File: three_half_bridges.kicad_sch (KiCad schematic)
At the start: 38 parts, among them J1 Conn_01x06_Pin, J2 Conn_01x06_Pin, J3 Conn_01x06_Pin, J4 Current Sense, J5 Conn_01x01_Socket, J6 Conn_01x01_Socket, J7 Conn_01x01_Socket, J8 Conn_01x01_Socket, J9 Conn_01x01_Socket, Q1 Q_NMOS_GDS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

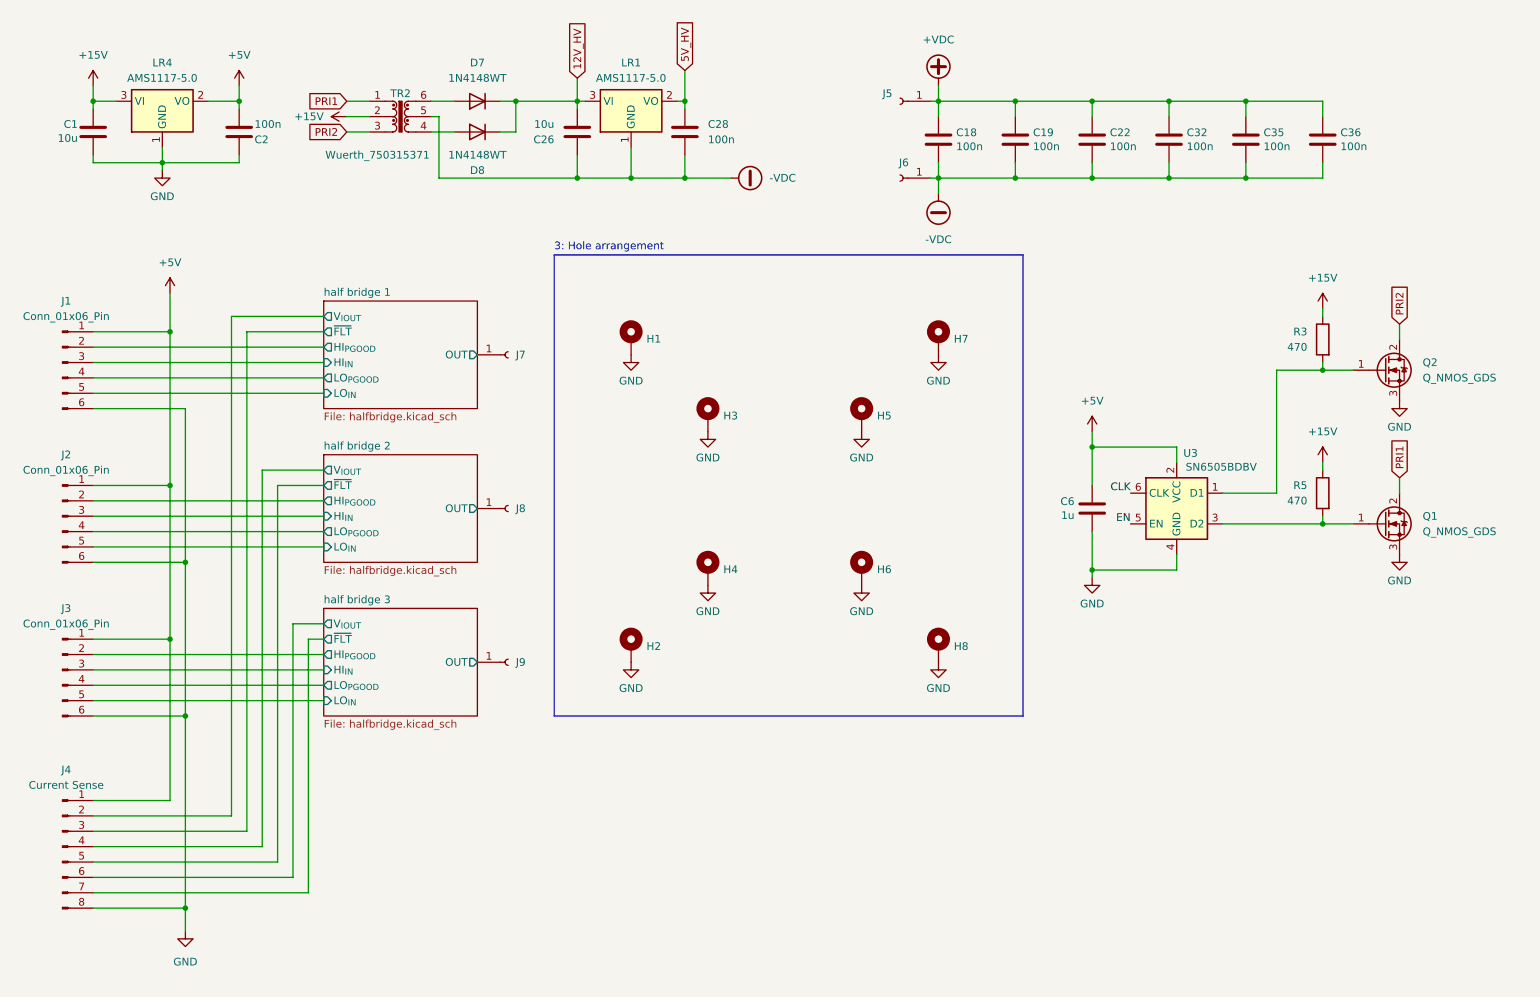
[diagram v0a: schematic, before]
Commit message: Updated LDO footrprint to use the SOT89 LM78L05 (issue 10); moved high side local regulators closer to digital isolator ICs (issue 10); pushed digital isolator ICs further to the allow room for LRs (issue 10); changed designator letter for zener diodes to Z to make it easier when hand soldering (issue 5) Updated footprints from placeholders (most of the diodes) to actual real component choices updated resistor values for BOM consolidation (220, 1k) moved resistor related to PGOOD for more optimal routing w/ minimal impact to function Changed structure of isolated driver design to use voltage doubler and 6505 or similar IC directly (issue 7,8,13) Only 5VDC is required for low voltage side, although several amps may be required depending on gate drive requirements Updated transformer footprint for more common 7.5mm by 2.5mm spacing, several 1:1.1 to 1:1.5 transformers are avilable with such spacing (issue 7) Moved Q8 designator back to correct place along with others that were mislocated somehow... Fixed placement of some footprints that were slightly off or not aligned to 0.25mm grid Replaced specific SO8 MOSFET driver with choose-your-own generic. I am personally using some cheapo LCSC TI 27523 clones (issue 11) added EVEN MORE VIAS!!!! thermal vias on not current sensitive pins to make soldering easier Added artwork (issue 6)
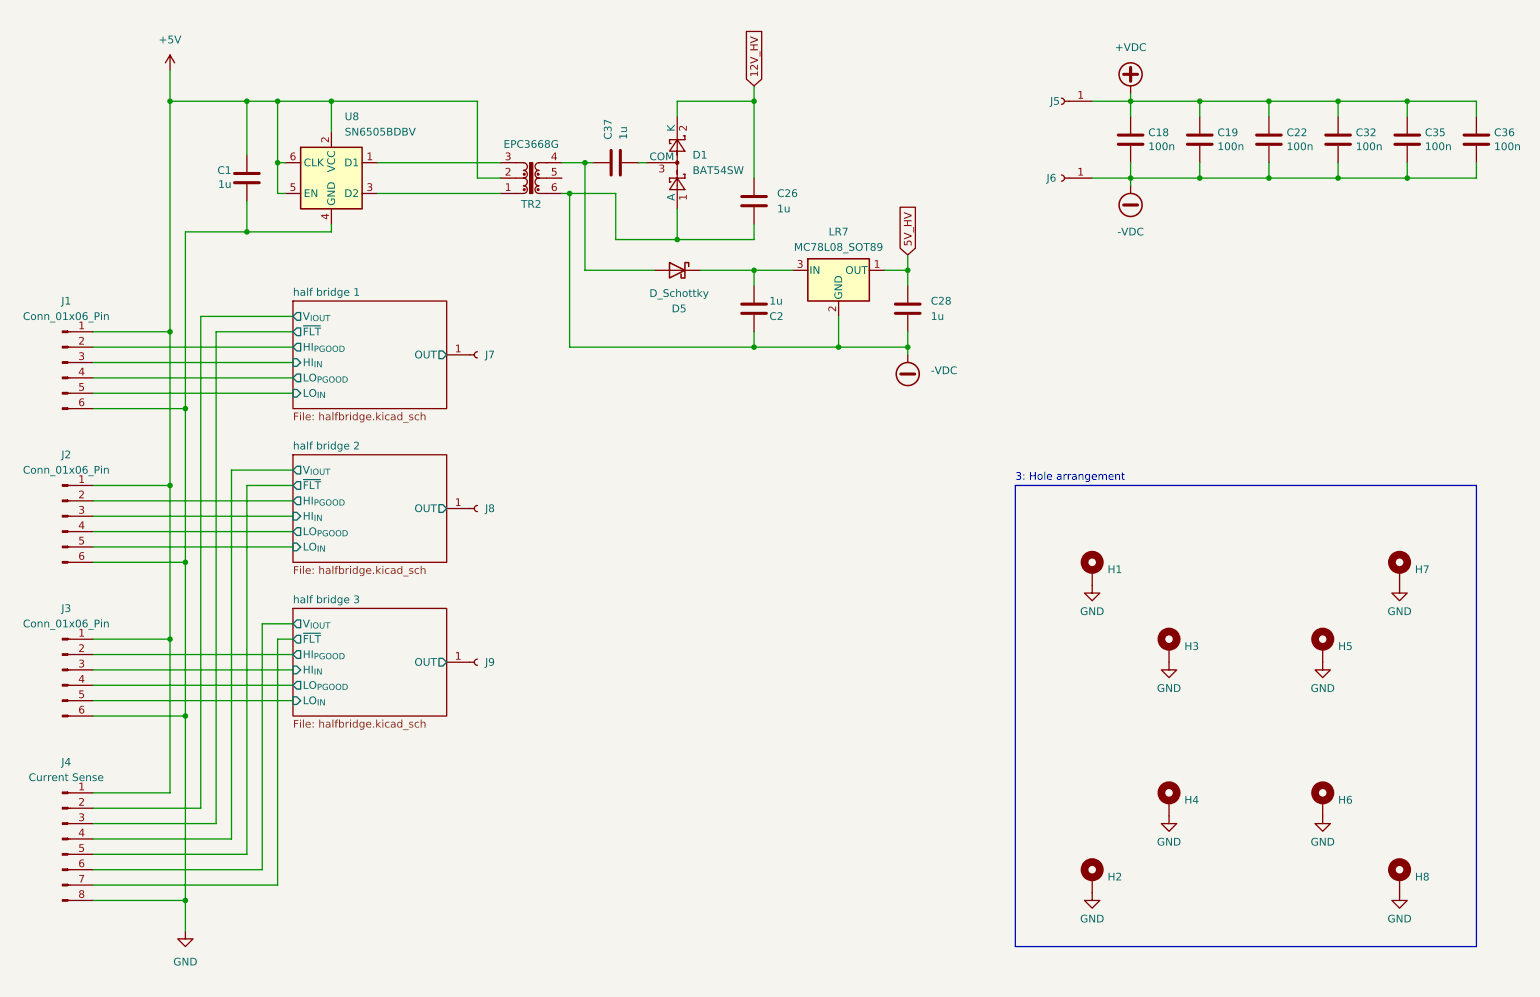
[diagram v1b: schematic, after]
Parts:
- removed C6: 1u, Capacitor_SMD:C_0805_2012Metric, symbol Device:C
- removed D7, D8: 1N4148WT, Diode_SMD:D_SOD-128, symbol Diode:1N4148WT
- removed LR1, LR4: AMS1117-5.0, Package_TO_SOT_SMD:SOT-89-3, symbol Regulator_Linear:AMS1117-5.0
- removed Q1, Q2: Q_NMOS_GDS, Package_TO_SOT_SMD:SOT-89-3, symbol Device:Q_NMOS_GDS
- removed R3, R5: 470, Resistor_SMD:R_0603_1608Metric, symbol Device:R
- removed U3: SN6505BDBV, Package_TO_SOT_SMD:SOT-23-6, symbol Power_Management:SN6505BDBV
- added C37: 1u, Capacitor_SMD:C_0603_1608Metric, symbol Device:C
- added D1: BAT54SW, Package_TO_SOT_SMD:SOT-323_SC-70, symbol Diode:BAT54SW
- added D5: D_Schottky, Diode_SMD:D_SOD-123, symbol Device:D_Schottky
- added LR7: MC78L08_SOT89, Package_TO_SOT_SMD:SOT-89-3, symbol Regulator_Linear:MC78L08_SOT89
- added U8: SN6505BDBV, Package_TO_SOT_SMD:SOT-23-6, symbol Power_Management:SN6505BDBV
- C1, C26: value 10u -> 1u; footprint Capacitor_SMD:C_0805_2012Metric -> Capacitor_SMD:C_0603_1608Metric
- C2, C28: value 100n -> 1u
- TR2: value Wuerth_750315371 -> EPC3668G; footprint Transformer_SMD:Transformer_Wuerth_750315371 -> Transformer_SMD:Pulse_PA2004NL
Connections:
- net +15V is gone; now on net +5V: C1.2, TR2.2
- net +5V: now also U8.2 (VCC), U8.5 (EN), U8.6 (CLK); no longer C2.2
- net -VDC: now also C2.1, C26.2, TR2.6, D1.1 (A), LR7.2 (GND); no longer C26.1, TR2.5
- net 12V_HV: now also C26.1, D1.2 (K); no longer C26.2
- net 5V_HV: now also LR7.1 (OUT)
- net GND: now also U8.4 (GND); no longer C2.1
- net at TR2.4: now also C37.1, D5.2 (A)
- net PRI1: no longer names the net of TR2.1
- net PRI1: now also U8.3 (D2)
- net PRI2: no longer names the net of TR2.3
- net PRI2: now also U8.1 (D1)
- new net: C2.2, D5.1 (K), LR7.3 (IN)
- new net: C37.2, D1.3 (COM)
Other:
- moved on the sheet: C1, C18, C19, C2, C22, C26, C28, C32, C35, C36, H1, H2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

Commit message: forgot to save and close prior to last commit
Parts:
- added J10: Conn_01x02_Pin, Connector_JST:JST_XH_B2B-XH-AM_1x02_P2.50mm_Vertical, symbol Connector:Conn_01x02_Pin
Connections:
- net +5V: now also J10.1 (Pin_1)
- net GND: now also J10.2 (Pin_2)
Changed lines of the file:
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@@
+	)
+	(junction
+		(at 40.64 46.99)
+		(diameter 0)
+		(color 0 0 0 0)
 	)
 	(junction
@@
 	(wire
 		(pts
+			(xy 25.4 25.4) (xy 38.1 25.4)
+		)
+		(stroke
+			(width 0)
+			(type default)
+		)
+	)
+	(wire
+		(pts
 			(xy 50.8 25.4) (xy 55.88 25.4)
 		)
@@
 	(wire
 		(pts
+			(xy 40.64 27.94) (xy 40.64 46.99)
+		)
+		(stroke
+			(width 0)
+			(type default)
+		)
+	)
+	(wire
+		(pts
 			(xy 25.4 99.06) (xy 58.42 99.06)
 		)
@@
 		(pts
 			(xy 40.64 76.2) (xy 40.64 101.6)
+		)
+		(stroke
+			(width 0)
+			(type default)
+		)
+	)
+	(wire
+		(pts
+			(xy 25.4 27.94) (xy 40.64 27.94)
 		)
 		(stroke
@@
 					(unit 1)
 				)
+			)
+		)
+	)
+	(symbol
+		(lib_id "Connector:Conn_01x02_Pin")
+		(at 20.32 25.4 0)
+		(unit 1)
+		(exclude_from_sim no)
+		(in_bom yes)
+		(on_board yes)
+		(dnp no)
+		(fields_autoplaced yes)
+		(property "Reference" "J10"
+			(at 20.955 20.32 0)
+			(effects
+				(font
+					(size 1.27 1.27)
+				)
+			)
+		)
+		(property "Value" "Conn_01x02_Pin"
+			(at 20.955 22.86 0)
+			(effects
+				(font
+					(size 1.27 1.27)
+				)
+			)
+		)
+		(property "Footprint" "Connector_JST:JST_XH_B2B-XH-AM_1x02_P2.50mm_Vertical"
+			(at 20.32 25.4 0)
+			(effects
+				(font
+					(size 1.27 1.27)
+				)
+				(hide yes)
+			)
+		)
+		(property "Datasheet" "~"
+			(at 20.32 25.4 0)
+			(effects
+				(font
+					(size 1.27 1.27)
+				)
+				(hide yes)
+			)
+		)
+		(property "Description" "Generic connector, single row, 01x02, script generated"
+			(at 20.32 25.4 0)
+			(effects
+				(font
+					(size 1.27 1.27)
+				)
+				(hide yes)
+			)
+		)
+		(pin "2"
+		)
+		(pin "1"
+		)
+		(instances
+			(project ""
+				(path "/93b08510-115c-4f21-9eb2-db10547c6f8e"
+					(reference "J10")
+					(unit 1)
+				)

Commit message: updated footprint for terminal blocks to use AMT0450028DB0000G‎
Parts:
- J5, J6, J7, J8, J9: footprint TerminalBlock_MetzConnect:TerminalBlock_MetzConnect_360425_1x01_Horizontal_ScrewM4.0_Boxed -> Library:AMT0450028DB0000G
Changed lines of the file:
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@@
 			)
 		)
-		(property "Footprint" "TerminalBlock_MetzConnect:TerminalBlock_MetzConnect_360425_1x01_Horizontal_ScrewM4.0_Boxed"
+		(property "Footprint" "Library:AMT0450028DB0000G"
 			(at 88.9 118.11 0)
 			(effects
@@
 			)
 		)
-		(property "Footprint" "TerminalBlock_MetzConnect:TerminalBlock_MetzConnect_360425_1x01_Horizontal_ScrewM4.0_Boxed"
+		(property "Footprint" "Library:AMT0450028DB0000G"
 			(at 88.9 92.71 0)
 			(effects
@@
 			)
 		)
-		(property "Footprint" "TerminalBlock_MetzConnect:TerminalBlock_MetzConnect_360425_1x01_Horizontal_ScrewM4.0_Boxed"
+		(property "Footprint" "Library:AMT0450028DB0000G"
 			(at 185.42 25.4 0)
 			(effects
@@
 			)
 		)
-		(property "Footprint" "TerminalBlock_MetzConnect:TerminalBlock_MetzConnect_360425_1x01_Horizontal_ScrewM4.0_Boxed"
+		(property "Footprint" "Library:AMT0450028DB0000G"
 			(at 185.42 38.1 0)
 			(effects
@@
 			)
 		)
-		(property "Footprint" "TerminalBlock_MetzConnect:TerminalBlock_MetzConnect_360425_1x01_Horizontal_ScrewM4.0_Boxed"
+		(property "Footprint" "Library:AMT0450028DB0000G"
 			(at 88.9 67.31 0)
 			(effects

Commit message: beginings of the implementation of the 10 open issues
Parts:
- LR7: value MC78L08_SOT89 -> MC78L05_SOT89
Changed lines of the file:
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@@
 			)
 		)
-		(property "Value" "MC78L08_SOT89"
+		(property "Value" "MC78L05_SOT89"
 			(at 148.59 49.53 0)
 			(effects
@@
 			)
 		)
-		(property "Description" "Positive 100mA 30V Linear Regulator, Fixed Output 8V, SOT-89"
+		(property "Description" "Positive 100mA 30V Linear Regulator, Fixed Output 5V, SOT-89"
 			(at 148.59 53.34 0)
 			(effects

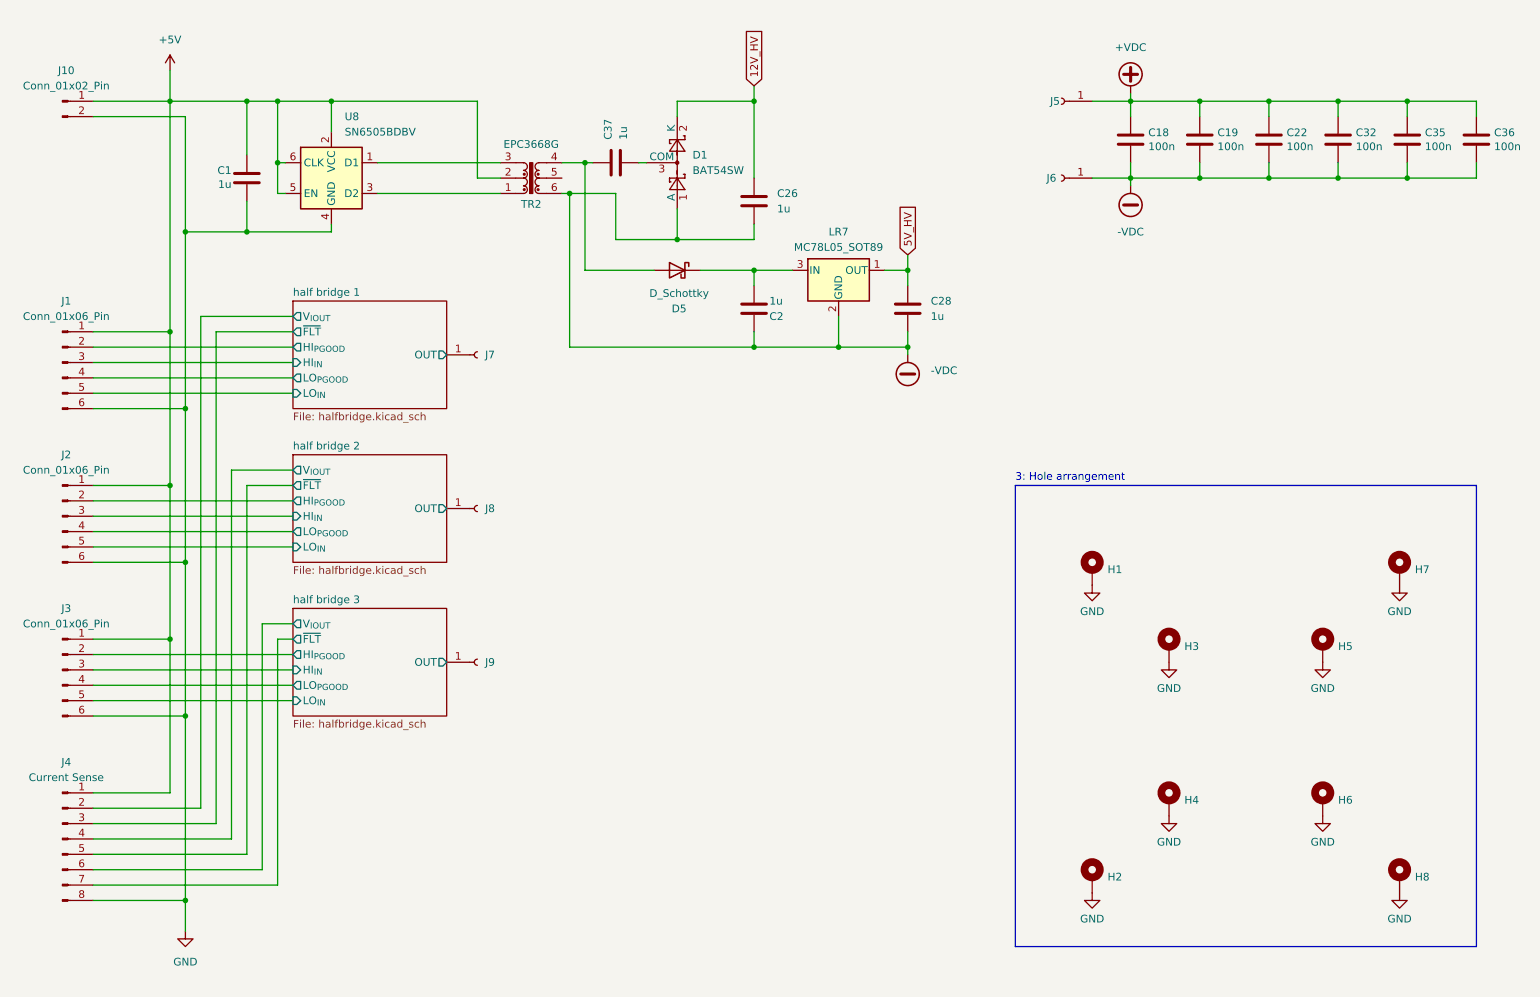
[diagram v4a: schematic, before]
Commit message: fixed many issues from previous itteration, added design rule checks to enforce minumum 2mm clearence between LV and HV side
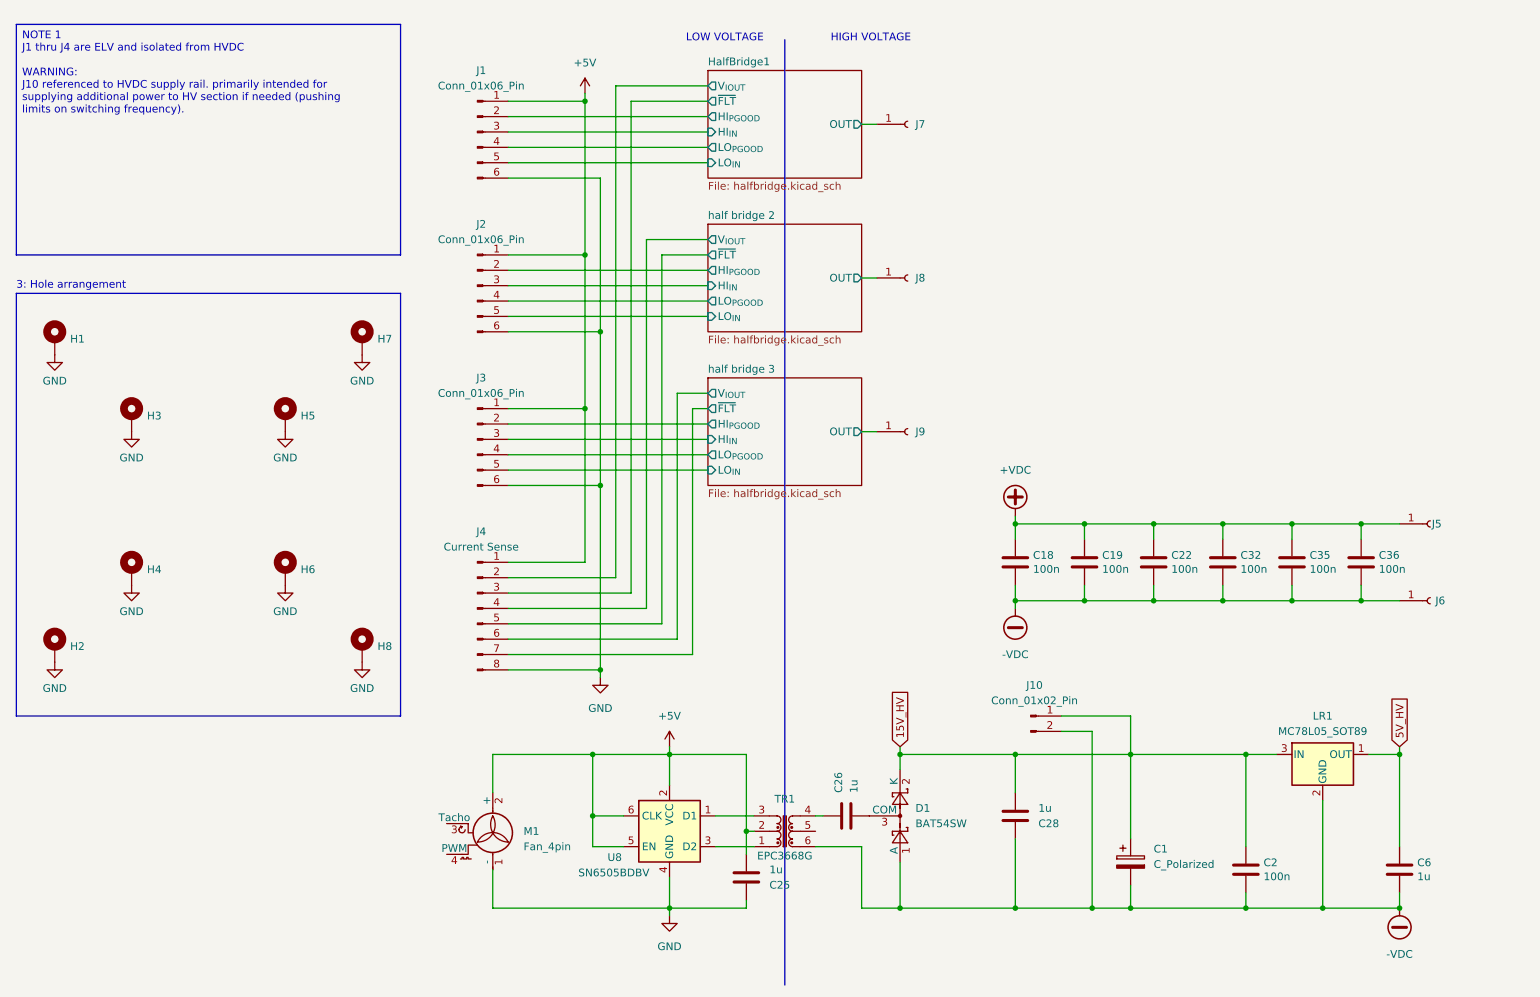
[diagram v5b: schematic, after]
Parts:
- removed C1, C37: 1u, Capacitor_SMD:C_0603_1608Metric, symbol Device:C
- removed D5: D_Schottky, Diode_SMD:D_SOD-123, symbol Device:D_Schottky
- removed LR7: MC78L05_SOT89, Package_TO_SOT_SMD:SOT-89-3, symbol Regulator_Linear:MC78L08_SOT89
- removed TR2: EPC3668G, Transformer_SMD:Pulse_PA2004NL, symbol Transformer:Wuerth_750315371
- added C1: C_Polarized, Capacitor_Tantalum_SMD:CP_EIA-6032-20_AVX-F, symbol Device:C_Polarized
- added C25: 1u, Capacitor_SMD:C_0603_1608Metric, symbol Device:C
- added C6: 1u, Capacitor_SMD:C_0805_2012Metric, symbol Device:C
- added LR1: MC78L05_SOT89, Package_TO_SOT_SMD:SOT-89-3, symbol Regulator_Linear:MC78L08_SOT89
- added M1: Fan_4pin, Connector_Molex:Molex_KK-254_AE-6410-04A_1x04_P2.54mm_Vertical, symbol Motor:Fan_4pin
- added TR1: EPC3668G, Transformer_SMD:Pulse_PA2004NL, symbol Transformer:Wuerth_750315371
- C2: value 1u -> 100n; footprint Capacitor_SMD:C_0603_1608Metric -> Capacitor_SMD:C_0805_2012Metric
- J10: footprint Connector_JST:JST_XH_B2B-XH-AM_1x02_P2.50mm_Vertical -> Connector_JST:JST_XH_B2B-XH-A_1x02_P2.50mm_Vertical
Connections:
- net +5V: now also C25.2, M1.2 (+), TR1.2; no longer J10.1 (Pin_1)
- net -VDC: now also C28.1, J10.2 (Pin_2), C1.2, C6.1, LR1.2 (GND), TR1.6; no longer C26.2, C28.2
- net 5V_HV: now also C6.2, LR1.1 (OUT); no longer C28.1
- net GND: now also C25.1, M1.1 (-); no longer J10.2 (Pin_2)
- net at U8.1 (D1): now also TR1.3
- net at U8.3 (D2): now also TR1.1
- net 15V_HV: now reaches C2.2
- net 15V_HV: now also C28.2, D1.2 (K), J10.1 (Pin_1), C1.1, LR1.3 (IN)
- net at D1.3 (COM): now also C26.2
- net 12V_HV: no longer names the net of C26.1
- net 12V_HV: now also TR1.4; no longer D1.2 (K)
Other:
- sheet half bridge 1 renamed HalfBridge1
- note added: "HIGH VOLTAGE"
- note added: "LOW VOLTAGE"
- moved on the sheet: C18, C19, C22, C32, C35, C36, H1, H2, H3, H4, H5, H6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
